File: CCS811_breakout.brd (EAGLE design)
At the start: 12.5 x 12.4 mm, 4 parts, among them U10 CCS811

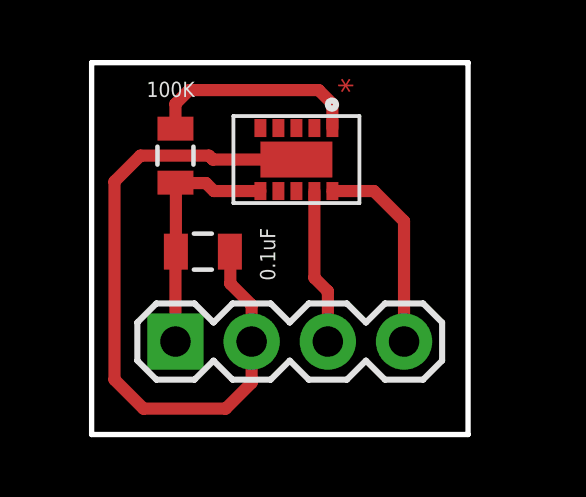
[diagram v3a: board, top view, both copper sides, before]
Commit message: Adjusted GND trace
Also changed board dimensions; added silkscreen
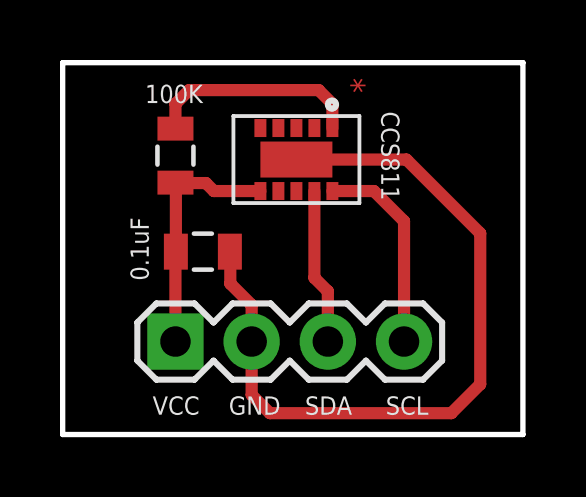
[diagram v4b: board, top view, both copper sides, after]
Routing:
- net GND: track 23.1 -> 25.5 mm
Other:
- board size 12.5 x 12.4 mm -> 15.3 x 12.4 mm
- board text added: "CCS811"
- board text added: "GND"
- board text added: "SCL"
- board text added: "SDA"
- board text added: "VCC"
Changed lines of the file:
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@@
 <board>
 <plain>
-<wire x1="0.254" y1="-0.4064" x2="12.8016" y2="-0.4064" width="0.1778" layer="20"/>
-<wire x1="12.8016" y1="-0.4064" x2="12.8016" y2="11.9888" width="0.1778" layer="20"/>
-<wire x1="12.8016" y1="11.9888" x2="0.254" y2="11.9888" width="0.1778" layer="20"/>
-<wire x1="0.254" y1="11.9888" x2="0.254" y2="-0.4064" width="0.1778" layer="20"/>
-<text x="8.4836" y="11.4808" size="0.8128" layer="1" font="vector" ratio="12" rot="R270">*</text>
+<wire x1="-0.7112" y1="-0.4064" x2="14.6304" y2="-0.4064" width="0.1778" layer="20"/>
+<wire x1="14.6304" y1="-0.4064" x2="14.6304" y2="11.9888" width="0.1778" layer="20"/>
+<wire x1="14.6304" y1="11.9888" x2="-0.7112" y2="11.9888" width="0.1778" layer="20"/>
+<wire x1="-0.7112" y1="11.9888" x2="-0.7112" y2="-0.4064" width="0.1778" layer="20"/>
+<text x="8.89" y="11.4808" size="0.8128" layer="1" font="vector" ratio="12" rot="R270">*</text>
+<text x="2.286" y="0.254" size="0.6096" layer="121" font="vector">VCC</text>
+<text x="4.826" y="0.254" size="0.6096" layer="121" font="vector">GND</text>
+<text x="7.366" y="0.254" size="0.6096" layer="121" font="vector">SDA</text>
+<text x="10.0584" y="0.254" size="0.6096" layer="121" font="vector">SCL</text>
+<text x="9.906" y="10.3632" size="0.6096" layer="121" font="vector" rot="SR270">CCS811</text>
 </plain>
 <attributes>
@@
 <attribute name="MPN" value="" x="3.9624" y="5.6896" size="1.778" layer="27" display="off"/>
 <attribute name="MF" value="" x="3.9624" y="5.6896" size="1.778" layer="27" display="off"/>
-<attribute name="VALUE" x="6.3754" y="4.7244" size="0.508" layer="121" font="vector" rot="R90"/>
+<attribute name="VALUE" x="2.159" y="4.7244" size="0.6096" layer="121" font="vector" rot="R90"/>
 </element>
 <element name="R2" library="SparkFun-Passives" package="0805" value="100K" x="3.048" y="8.89" smashed="yes" rot="R270">
@@
 <attribute name="MPN" value="" x="3.048" y="8.89" size="1.778" layer="27" rot="R270" display="off"/>
 <attribute name="MF" value="" x="3.048" y="8.89" size="1.778" layer="27" rot="R270" display="off"/>
-<attribute name="VALUE" x="2.0828" y="10.8458" size="0.508" layer="121" font="vector"/>
+<attribute name="VALUE" x="2.032" y="10.6426" size="0.6096" layer="121" font="vector"/>
 </element>
 <element name="J1" library="SparkFun-Connectors" package="1X04" value="" x="3.048" y="2.6924" smashed="yes">
@@
 <wire x1="4.8768" y1="4.6228" x2="4.8768" y2="5.6752" width="0.4064" layer="1"/>
 <wire x1="4.8768" y1="5.6752" x2="4.8624" y2="5.6896" width="0.4064" layer="1"/>
-<wire x1="7.08" y1="8.7592" x2="4.2964" y2="8.7592" width="0.4064" layer="1"/>
-<wire x1="4.2964" y1="8.7592" x2="4.1656" y2="8.89" width="0.4064" layer="1"/>
-<wire x1="4.1656" y1="8.89" x2="1.8796" y2="8.89" width="0.4064" layer="1"/>
-<wire x1="1.8796" y1="8.89" x2="1.016" y2="8.0264" width="0.4064" layer="1"/>
-<wire x1="1.016" y1="8.0264" x2="1.016" y2="1.4224" width="0.4064" layer="1"/>
-<wire x1="1.016" y1="1.4224" x2="1.9812" y2="0.4572" width="0.4064" layer="1"/>
-<wire x1="1.9812" y1="0.4572" x2="4.7244" y2="0.4572" width="0.4064" layer="1"/>
-<wire x1="4.7244" y1="0.4572" x2="5.588" y2="1.3208" width="0.4064" layer="1"/>
-<wire x1="5.588" y1="1.3208" x2="5.588" y2="2.6924" width="0.4064" layer="1"/>
+<wire x1="7.08" y1="8.7592" x2="10.748" y2="8.7592" width="0.4064" layer="1"/>
+<wire x1="10.748" y1="8.7592" x2="13.208" y2="6.2992" width="0.4064" layer="1"/>
+<wire x1="13.208" y1="6.2992" x2="13.208" y2="1.27" width="0.4064" layer="1"/>
+<wire x1="13.208" y1="1.27" x2="12.2428" y2="0.3048" width="0.4064" layer="1"/>
+<wire x1="12.2428" y1="0.3048" x2="6.1976" y2="0.3048" width="0.4064" layer="1"/>
+<wire x1="6.1976" y1="0.3048" x2="5.588" y2="0.9144" width="0.4064" layer="1"/>
+<wire x1="5.588" y1="0.9144" x2="5.588" y2="2.6924" width="0.4064" layer="1"/>
 </signal>
 <signal name="VCC">

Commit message: Adjusted board dimensions
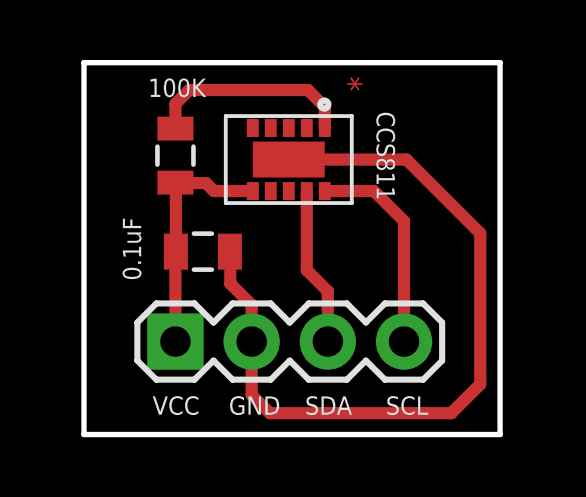
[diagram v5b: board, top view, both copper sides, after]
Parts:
- moved U10 0.25 mm to (4.83, 10.1)
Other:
- board size 15.3 x 12.4 mm -> 13.9 x 12.4 mm
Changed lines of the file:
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@@
 <board>
 <plain>
-<wire x1="-0.7112" y1="-0.4064" x2="14.6304" y2="-0.4064" width="0.1778" layer="20"/>
-<wire x1="14.6304" y1="-0.4064" x2="14.6304" y2="11.9888" width="0.1778" layer="20"/>
-<wire x1="14.6304" y1="11.9888" x2="-0.7112" y2="11.9888" width="0.1778" layer="20"/>
-<wire x1="-0.7112" y1="11.9888" x2="-0.7112" y2="-0.4064" width="0.1778" layer="20"/>
-<text x="8.89" y="11.4808" size="0.8128" layer="1" font="vector" ratio="12" rot="R270">*</text>
+<wire x1="0" y1="-0.4064" x2="13.8684" y2="-0.4064" width="0.1778" layer="20"/>
+<wire x1="13.8684" y1="-0.4064" x2="13.8684" y2="11.9888" width="0.1778" layer="20"/>
+<wire x1="13.8684" y1="11.9888" x2="0" y2="11.9888" width="0.1778" layer="20"/>
+<wire x1="0" y1="11.9888" x2="0" y2="-0.4064" width="0.1778" layer="20"/>
+<text x="8.7884" y="11.5316" size="0.8128" layer="1" font="vector" ratio="12" rot="R270">*</text>
 <text x="2.286" y="0.254" size="0.6096" layer="121" font="vector">VCC</text>
 <text x="4.826" y="0.254" size="0.6096" layer="121" font="vector">GND</text>
 <text x="7.366" y="0.254" size="0.6096" layer="121" font="vector">SDA</text>
 <text x="10.0584" y="0.254" size="0.6096" layer="121" font="vector">SCL</text>
-<text x="9.906" y="10.3632" size="0.6096" layer="121" font="vector" rot="SR270">CCS811</text>
+<text x="9.7536" y="10.3632" size="0.6096" layer="121" font="vector" rot="SR270">CCS811</text>
 </plain>
 <attributes>
@@
 </autorouter>
 <elements>
-<element name="U10" library="CCS811" package="LGA" value="CCS811" x="5.08" y="10.1092" smashed="yes" rot="R270"/>
+<element name="U10" library="CCS811" package="LGA" value="CCS811" x="4.826" y="10.1092" smashed="yes" rot="R270"/>
 <element name="C5" library="SparkFun-Passives" package="0805" value="0.1uF" x="3.9624" y="5.6896" smashed="yes">
 <attribute name="OC_NEWARK" value="unknown" x="3.9624" y="5.6896" size="1.778" layer="27" display="off"/>
 <attribute name="MPN" value="" x="3.9624" y="5.6896" size="1.778" layer="27" display="off"/>
 <attribute name="MF" value="" x="3.9624" y="5.6896" size="1.778" layer="27" display="off"/>
-<attribute name="VALUE" x="2.159" y="4.7244" size="0.6096" layer="121" font="vector" rot="R90"/>
+<attribute name="VALUE" x="1.905" y="4.7244" size="0.6096" layer="121" font="vector" rot="R90"/>
 </element>
 <element name="R2" library="SparkFun-Passives" package="0805" value="100K" x="3.048" y="8.89" smashed="yes" rot="R270">
@@
 <attribute name="MPN" value="" x="3.048" y="8.89" size="1.778" layer="27" rot="R270" display="off"/>
 <attribute name="MF" value="" x="3.048" y="8.89" size="1.778" layer="27" rot="R270" display="off"/>
-<attribute name="VALUE" x="2.032" y="10.6426" size="0.6096" layer="121" font="vector"/>
+<attribute name="VALUE" x="2.1336" y="10.8458" size="0.6096" layer="121" font="vector"/>
 </element>
 <element name="J1" library="SparkFun-Connectors" package="1X04" value="" x="3.048" y="2.6924" smashed="yes">
@@
 <wire x1="4.8768" y1="4.6228" x2="4.8768" y2="5.6752" width="0.4064" layer="1"/>
 <wire x1="4.8768" y1="5.6752" x2="4.8624" y2="5.6896" width="0.4064" layer="1"/>
-<wire x1="7.08" y1="8.7592" x2="10.748" y2="8.7592" width="0.4064" layer="1"/>
 <wire x1="10.748" y1="8.7592" x2="13.208" y2="6.2992" width="0.4064" layer="1"/>
 <wire x1="13.208" y1="6.2992" x2="13.208" y2="1.27" width="0.4064" layer="1"/>
@@
 <wire x1="6.1976" y1="0.3048" x2="5.588" y2="0.9144" width="0.4064" layer="1"/>
 <wire x1="5.588" y1="0.9144" x2="5.588" y2="2.6924" width="0.4064" layer="1"/>
+<wire x1="6.826" y1="8.7592" x2="10.748" y2="8.7592" width="0.4064" layer="1"/>
 </signal>
 <signal name="VCC">
@@
 <wire x1="3.048" y1="5.6752" x2="3.0624" y2="5.6896" width="0.4064" layer="1"/>
 <wire x1="3.0624" y1="5.6896" x2="3.0624" y2="7.9756" width="0.4064" layer="1"/>
-<wire x1="5.88" y1="7.7092" x2="4.3304" y2="7.7092" width="0.4064" layer="1"/>
 <wire x1="4.3304" y1="7.7092" x2="4.064" y2="7.9756" width="0.4064" layer="1"/>
 <wire x1="4.064" y1="7.9756" x2="3.0624" y2="7.9756" width="0.4064" layer="1"/>
 <wire x1="3.0624" y1="7.9756" x2="3.048" y2="7.99" width="0.4064" layer="1"/>
+<wire x1="4.3304" y1="7.7092" x2="5.626" y2="7.7092" width="0.4064" layer="1"/>
 </signal>
 <signal name="SCL">
 <contactref element="U10" pad="10"/>
 <contactref element="J1" pad="4"/>
-<wire x1="8.28" y1="7.7092" x2="9.6644" y2="7.7092" width="0.4064" layer="1"/>
 <wire x1="9.6644" y1="7.7092" x2="10.668" y2="6.7056" width="0.4064" layer="1"/>
 <wire x1="10.668" y1="6.7056" x2="10.668" y2="2.6924" width="0.4064" layer="1"/>
+<wire x1="8.026" y1="7.7092" x2="9.6644" y2="7.7092" width="0.4064" layer="1"/>
 </signal>
 <signal name="SDA">
 <contactref element="U10" pad="9"/>
 <contactref element="J1" pad="3"/>
-<wire x1="7.68" y1="7.7092" x2="7.68" y2="4.8168" width="0.4064" layer="1"/>
-<wire x1="7.68" y1="4.8168" x2="8.128" y2="4.3688" width="0.4064" layer="1"/>
 <wire x1="8.128" y1="4.3688" x2="8.128" y2="2.6924" width="0.4064" layer="1"/>
+<wire x1="7.426" y1="7.7092" x2="7.426" y2="5.0708" width="0.4064" layer="1"/>
+<wire x1="7.426" y1="5.0708" x2="8.128" y2="4.3688" width="0.4064" layer="1"/>
 </signal>
 <signal name="N$1">
@@
 <wire x1="3.048" y1="9.79" x2="3.048" y2="10.6172" width="0.4064" layer="1"/>
 <wire x1="3.048" y1="10.6172" x2="3.5052" y2="11.0744" width="0.4064" layer="1"/>
-<wire x1="8.28" y1="9.8092" x2="8.28" y2="10.6176" width="0.4064" layer="1"/>
-<wire x1="8.28" y1="10.6176" x2="7.8232" y2="11.0744" width="0.4064" layer="1"/>
-<wire x1="7.8232" y1="11.0744" x2="3.5052" y2="11.0744" width="0.4064" layer="1"/>
+<wire x1="8.026" y1="9.8092" x2="8.026" y2="10.516" width="0.4064" layer="1"/>
+<wire x1="8.026" y1="10.516" x2="7.4676" y2="11.0744" width="0.4064" layer="1"/>
+<wire x1="7.4676" y1="11.0744" x2="3.5052" y2="11.0744" width="0.4064" layer="1"/>
 </signal>
 </signals>

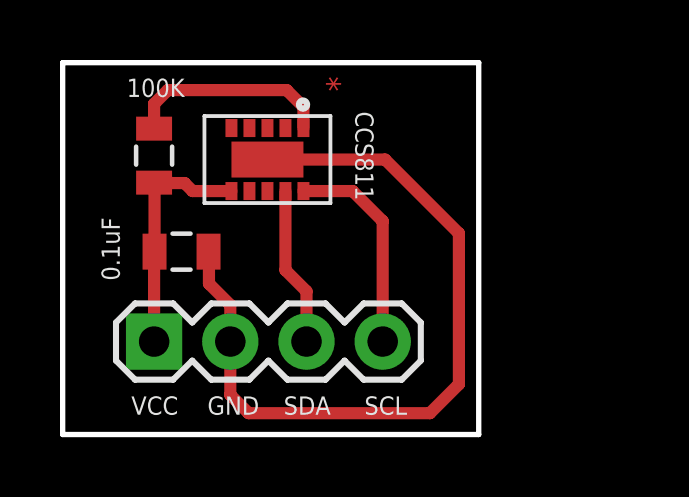
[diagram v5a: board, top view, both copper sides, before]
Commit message: Broken essential pins out
INT and WAKE pins are now broken out
Updated capacitor to 1uF as recommended by datasheet
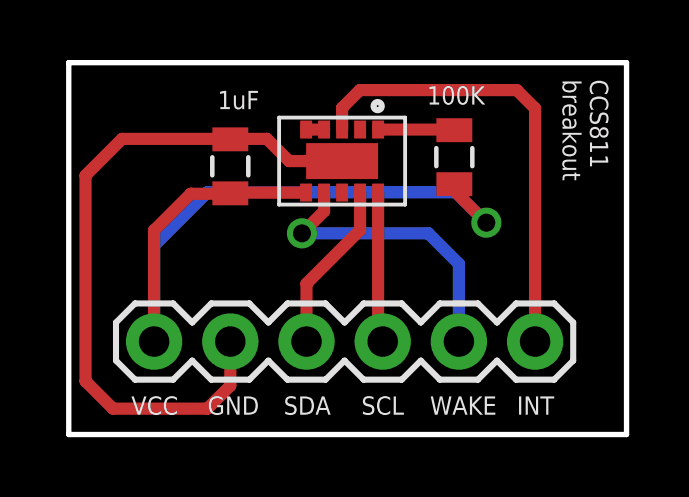
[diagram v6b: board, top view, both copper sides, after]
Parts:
- C5: value 0.1uF -> 1uF
- J1: device SparkFun-Connectors:1X04 -> SparkFun-Connectors:1X06
- moved R2 10.0 mm to (13.1, 8.84)
- moved C5 3.28 mm to (5.59, 8.53), turned to 90 degrees
- moved U10 2.49 mm to (7.32, 10.1)
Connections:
- new net INT: J1.6, U10.3
- new net N$2: U10.4, U10.5
- new net WAKE: J1.5, U10.7
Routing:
- net VCC: track 7.98 -> 26.5 mm, vias 0 -> 1
- net INT: track 0.00 -> 15.4 mm
- net WAKE: track 0.00 -> 9.91 mm, vias 0 -> 1
- net N$1: track 6.93 -> 2.55 mm
- net GND: track 25.8 -> 23.2 mm
- net SCL: track 7.07 -> 5.03 mm
- net N$2: track 0.00 -> 0.60 mm
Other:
- board size 13.9 x 12.4 mm -> 18.6 x 12.4 mm
- board text added: "AKstudios"
- board text added: "CCS811 breakout"
- board text added: "Designed by"
- board text added: "INT"
- board text added: "WAKE"
- board text removed: "*"
- board text removed: "CCS811"

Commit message: Adjusted traces
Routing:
- net WAKE: track 9.91 -> 14.4 mm
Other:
- board size 18.6 x 12.4 mm -> 18.4 x 12.4 mm
- board text added: "CCS811"
- board text removed: "CCS811 breakout"
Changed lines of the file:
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@@
 <board>
 <plain>
-<wire x1="0.2032" y1="-0.4064" x2="18.796" y2="-0.4064" width="0.1778" layer="20"/>
-<wire x1="18.796" y1="-0.4064" x2="18.796" y2="11.9888" width="0.1778" layer="20"/>
-<wire x1="18.796" y1="11.9888" x2="0.2032" y2="11.9888" width="0.1778" layer="20"/>
+<wire x1="0.2032" y1="-0.4064" x2="18.5928" y2="-0.4064" width="0.1778" layer="20"/>
+<wire x1="18.5928" y1="-0.4064" x2="18.5928" y2="11.9888" width="0.1778" layer="20"/>
+<wire x1="18.5928" y1="11.9888" x2="0.2032" y2="11.9888" width="0.1778" layer="20"/>
 <wire x1="0.2032" y1="11.9888" x2="0.2032" y2="-0.4064" width="0.1778" layer="20"/>
 <text x="2.286" y="0.254" size="0.6096" layer="121" font="vector">VCC</text>
@@
 <text x="7.366" y="0.254" size="0.6096" layer="121" font="vector">SDA</text>
 <text x="9.9568" y="0.254" size="0.6096" layer="121" font="vector">SCL</text>
-<text x="16.6624" y="11.43" size="0.6096" layer="121" font="vector" rot="SR270">CCS811
-breakout</text>
+<text x="7.7216" y="6.0452" size="0.6096" layer="121" font="vector" rot="SR0">CCS811</text>
 <text x="12.2428" y="0.254" size="0.6096" layer="121" font="vector">WAKE</text>
 <text x="15.1384" y="0.254" size="0.6096" layer="121" font="vector">INT</text>
-<text x="6.7564" y="10.7188" size="0.6096" layer="122" font="vector" rot="SMR0">Designed by</text>
-<text x="6.8072" y="9.4996" size="0.8128" layer="122" font="vector" ratio="15" rot="SMR0">AKstudios</text>
+<text x="12.2936" y="8.7884" size="0.6096" layer="122" font="vector" rot="SMR0">Designed by</text>
+<text x="12.446" y="7.5692" size="0.8128" layer="122" font="vector" ratio="15" rot="SMR0">AKstudios</text>
 </plain>
 <attributes>
@@
 <wire x1="5.6024" y1="9.4488" x2="5.588" y2="9.4344" width="0.4064" layer="1"/>
 <wire x1="5.588" y1="2.6924" x2="5.588" y2="1.2192" width="0.4064" layer="1"/>
-<wire x1="5.588" y1="1.2192" x2="4.826" y2="0.4572" width="0.4064" layer="1"/>
-<wire x1="4.826" y1="0.4572" x2="1.6764" y2="0.4572" width="0.4064" layer="1"/>
-<wire x1="1.6764" y1="0.4572" x2="0.762" y2="1.3716" width="0.4064" layer="1"/>
-<wire x1="0.762" y1="1.3716" x2="0.762" y2="8.2296" width="0.4064" layer="1"/>
-<wire x1="0.762" y1="8.2296" x2="1.9812" y2="9.4488" width="0.4064" layer="1"/>
-<wire x1="1.9812" y1="9.4488" x2="5.5736" y2="9.4488" width="0.4064" layer="1"/>
+<wire x1="5.588" y1="1.2192" x2="4.7752" y2="0.4064" width="0.4064" layer="1"/>
+<wire x1="1.9304" y1="9.4488" x2="5.5736" y2="9.4488" width="0.4064" layer="1"/>
 <wire x1="5.5736" y1="9.4488" x2="5.588" y2="9.4344" width="0.4064" layer="1"/>
+<wire x1="1.9304" y1="9.4488" x2="1.1176" y2="8.636" width="0.4064" layer="1"/>
+<wire x1="1.1176" y1="8.636" x2="1.1176" y2="1.2192" width="0.4064" layer="1"/>
+<wire x1="1.1176" y1="1.2192" x2="1.9304" y2="0.4064" width="0.4064" layer="1"/>
+<wire x1="1.9304" y1="0.4064" x2="4.7752" y2="0.4064" width="0.4064" layer="1"/>
 </signal>
 <signal name="VCC">
@@
 <contactref element="J1" pad="5"/>
 <contactref element="U10" pad="7"/>
+<via x="5.7404" y="6.2992" extent="1-16" drill="0.6"/>
+<wire x1="5.7404" y1="6.2992" x2="12.192" y2="6.2992" width="0.4064" layer="16"/>
+<wire x1="12.192" y1="6.2992" x2="13.208" y2="5.2832" width="0.4064" layer="16"/>
+<wire x1="13.208" y1="5.2832" x2="13.208" y2="2.6924" width="0.4064" layer="16"/>
 <wire x1="8.7152" y1="7.6584" x2="8.7152" y2="7.0388" width="0.4064" layer="1"/>
 <wire x1="8.7152" y1="7.0388" x2="7.9756" y2="6.2992" width="0.4064" layer="1"/>
-<via x="7.9756" y="6.2992" extent="1-16" drill="0.6"/>
-<wire x1="7.9756" y1="6.2992" x2="12.192" y2="6.2992" width="0.4064" layer="16"/>
-<wire x1="12.192" y1="6.2992" x2="13.208" y2="5.2832" width="0.4064" layer="16"/>
-<wire x1="13.208" y1="5.2832" x2="13.208" y2="2.6924" width="0.4064" layer="16"/>
+<wire x1="7.9756" y1="6.2992" x2="5.7404" y2="6.2992" width="0.4064" layer="1"/>
 </signal>
 <signal name="INT">
@@
 </board>
 </drawing>
-<compatibility>
-<note version="6.3" minversion="6.2.2" severity="warning">
-Since Version 6.2.2 text objects can contain more than one line,
-which will not be processed correctly with this version.
-</note>
-</compatibility>
 </eagle>
